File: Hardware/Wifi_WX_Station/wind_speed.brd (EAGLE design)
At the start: 25.5 x 25.4 mm, 10 parts, among them T1 MMBT3904

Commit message: backup
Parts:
- OPTO1: value OSRAM_SHF9201 -> OSRAM_SFH9201
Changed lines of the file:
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@@
 <?xml version="1.0" encoding="utf-8"?>
 <!DOCTYPE eagle SYSTEM "eagle.dtd">
-<eagle version="6.3">
+<eagle version="6.5.0">
 <drawing>
 <settings>
@@
 </autorouter>
 <elements>
-<element name="OPTO1" library="wifi_WX" package="OSRAM-6" value="OSRAM_SHF9201" x="7.62" y="15.24" smashed="yes" rot="R180">
+<element name="OPTO1" library="wifi_WX" package="OSRAM-6" value="OSRAM_SFH9201" x="7.62" y="15.24" smashed="yes" rot="R180">
 <attribute name="NAME" x="10.795" y="10.795" size="1.27" layer="25" rot="R90"/>
 </element>

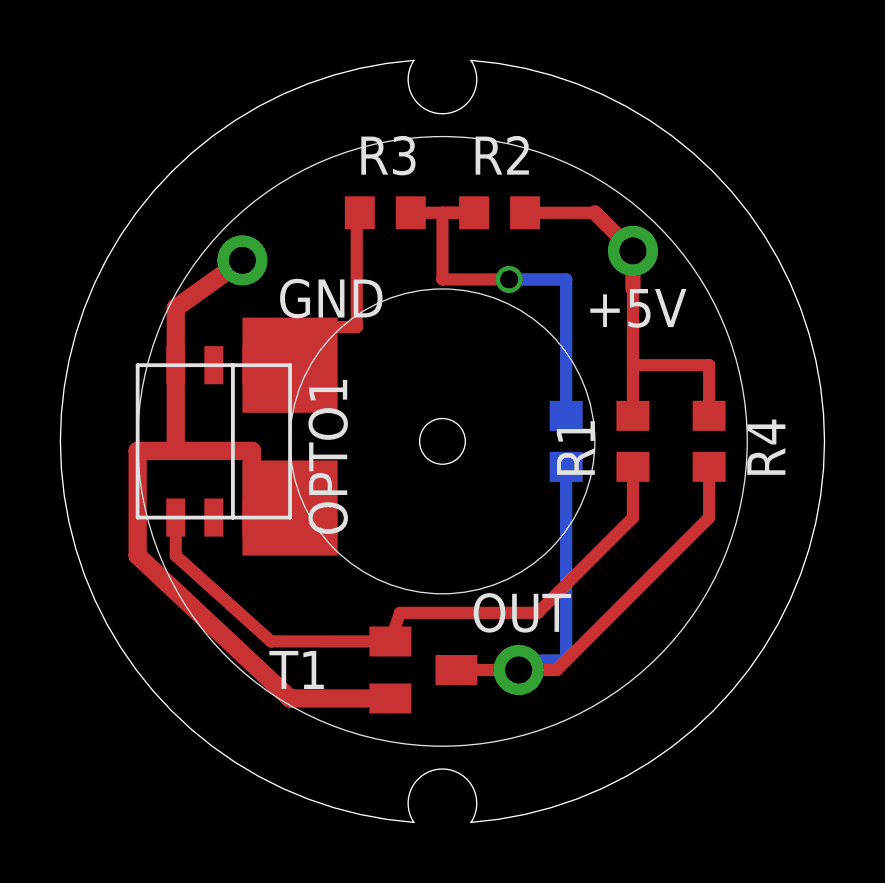
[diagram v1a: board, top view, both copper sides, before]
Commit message: added PCB for BOSH PMP180 revised WE28 schemaitc with added text
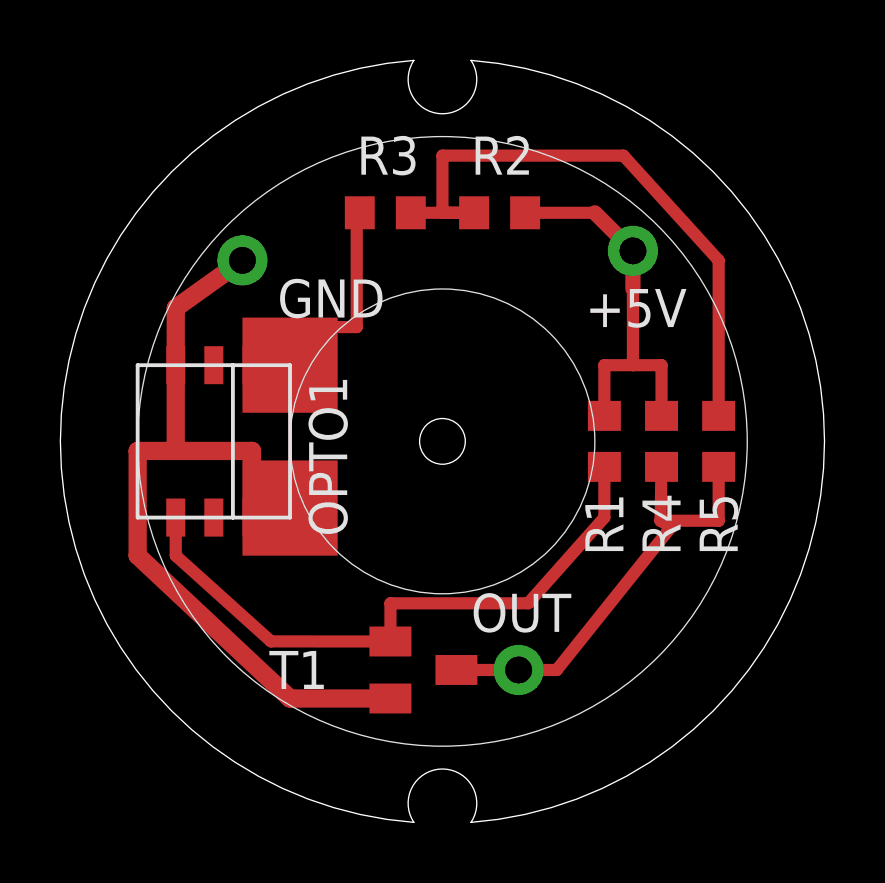
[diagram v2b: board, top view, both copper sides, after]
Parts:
- moved R5 5.08 mm to (23.2, 14.0), flipped to the top
- moved R4 1.59 mm to (21.3, 14.0)
- moved R1 0.95 mm to (19.4, 14.0)
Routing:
- net N$6: track 14.1 -> 21.0 mm, vias 1 -> 0
- net N$4: track 20.6 -> 15.4 mm
- net N$3: track 13.9 -> 13.2 mm
